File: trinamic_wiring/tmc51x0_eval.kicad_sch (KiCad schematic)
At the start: 0 parts

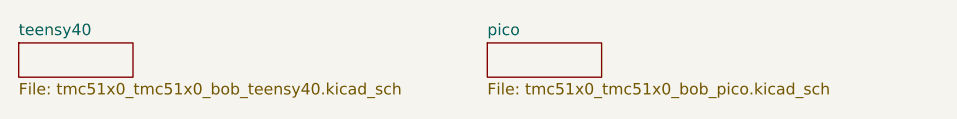
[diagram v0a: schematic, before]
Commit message: Add eval board
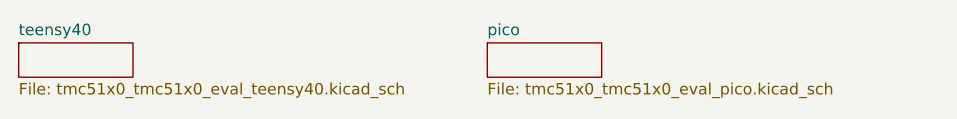
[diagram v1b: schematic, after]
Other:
- sheet pico: file tmc51x0_tmc51x0_bob_pico.kicad_sch -> tmc51x0_tmc51x0_eval_pico.kicad_sch
- sheet teensy40: file tmc51x0_tmc51x0_bob_teensy40.kicad_sch -> tmc51x0_tmc51x0_eval_teensy40.kicad_sch
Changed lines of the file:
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@@
       (effects (font (size 1.27 1.27)) (justify left bottom))
     )
-    (property "Sheetfile" "tmc51x0_tmc51x0_bob_teensy40.kicad_sch" (at 110.49 64.0846 0)
+    (property "Sheetfile" "tmc51x0_tmc51x0_eval_teensy40.kicad_sch" (at 110.49 64.0846 0)
       (effects (font (size 1.27 1.27)) (justify left top))
     )
     (instances
       (project "trinamic_wiring"
-        (path "/e4144788-6304-493f-818e-5d881d3b7418/a161638e-a96f-4455-865a-1d7502675f43/176cb0b5-cab1-47ac-9998-e59b71e39393" (page "27"))
+        (path "/e4144788-6304-493f-818e-5d881d3b7418/a161638e-a96f-4455-865a-1d7502675f43/b07f1639-ae99-4e69-a4ff-b15d0c967980" (page "20"))
       )
     )
@@
       (effects (font (size 1.27 1.27)) (justify left bottom))
     )
-    (property "Sheetfile" "tmc51x0_tmc51x0_bob_pico.kicad_sch" (at 162.56 64.0846 0)
+    (property "Sheetfile" "tmc51x0_tmc51x0_eval_pico.kicad_sch" (at 162.56 64.0846 0)
       (effects (font (size 1.27 1.27)) (justify left top))
     )
     (instances
       (project "trinamic_wiring"
-        (path "/e4144788-6304-493f-818e-5d881d3b7418/a161638e-a96f-4455-865a-1d7502675f43/176cb0b5-cab1-47ac-9998-e59b71e39393" (page "17"))
+        (path "/e4144788-6304-493f-818e-5d881d3b7418/a161638e-a96f-4455-865a-1d7502675f43/b07f1639-ae99-4e69-a4ff-b15d0c967980" (page "21"))
       )
     )

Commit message: Deleted sheet and updated comment on another
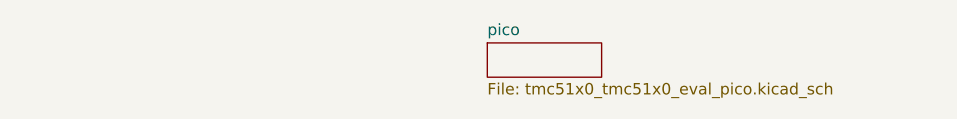
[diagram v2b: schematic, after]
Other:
- removed sheet teensy40
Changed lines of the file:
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@@
     (date "2024-06-13")
-  )
-  (sheet (at 110.49 59.69) (size 12.7 3.81) (fields_autoplaced)
-    (stroke (width 0.1524) (type solid))
-    (fill (color 0 0 0 0.0000))
-    (property "Sheetname" "teensy40" (at 110.49 58.9784 0)
-      (effects (font (size 1.27 1.27)) (justify left bottom))
-    )
-    (property "Sheetfile" "tmc51x0_tmc51x0_eval_teensy40.kicad_sch" (at 110.49 64.0846 0)
-      (effects (font (size 1.27 1.27)) (justify left top))
-    )
-    (instances
-      (project "trinamic_wiring"
-        (path "/e4144788-6304-493f-818e-5d881d3b7418/a161638e-a96f-4455-865a-1d7502675f43/b07f1639-ae99-4e69-a4ff-b15d0c967980" (page "20"))
-      )
-    )
   )
   (sheet (at 162.56 59.69) (size 12.7 3.81) (fields_autoplaced)
